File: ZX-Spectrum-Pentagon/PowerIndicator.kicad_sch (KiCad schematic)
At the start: 6 parts

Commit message: prepare for pcb
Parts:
- DPI1: value (none) -> RED; footprint (none) -> LED_SMD:LED_0805_2012Metric_Pad1.15x1.40mm_HandSolder
- DPI2: value (none) -> YELLO; footprint (none) -> LED_SMD:LED_0805_2012Metric_Pad1.15x1.40mm_HandSolder
- DPI3: value (none) -> GREEN; footprint (none) -> LED_SMD:LED_0805_2012Metric_Pad1.15x1.40mm_HandSolder
- RPI1, RPI2, RPI3: value (none) -> 330; footprint (none) -> Resistor_SMD:R_0805_2012Metric_Pad1.20x1.40mm_HandSolder
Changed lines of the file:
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@@
       (effects (font (size 1.27 1.27)) (justify left))
     )
-    (property "Value" "" (id 1) (at 39.878 70.993 0)
+    (property "Value" "330" (id 1) (at 39.878 70.993 0)
       (effects (font (size 1.27 1.27)) (justify left))
     )
-    (property "Footprint" "" (id 2) (at 36.322 69.85 90)
+    (property "Footprint" "Resistor_SMD:R_0805_2012Metric_Pad1.20x1.40mm_HandSolder" (id 2) (at 36.322 69.85 90)
       (effects (font (size 1.27 1.27)) hide)
     )
@@
       (effects (font (size 1.27 1.27)) (justify left))
     )
-    (property "Value" "" (id 1) (at 52.578 70.993 0)
+    (property "Value" "330" (id 1) (at 52.578 70.993 0)
       (effects (font (size 1.27 1.27)) (justify left))
     )
-    (property "Footprint" "" (id 2) (at 49.022 69.85 90)
+    (property "Footprint" "Resistor_SMD:R_0805_2012Metric_Pad1.20x1.40mm_HandSolder" (id 2) (at 49.022 69.85 90)
       (effects (font (size 1.27 1.27)) hide)
     )
@@
       (effects (font (size 1.27 1.27)) (justify left))
     )
-    (property "Value" "" (id 1) (at 65.278 70.993 0)
+    (property "Value" "330" (id 1) (at 65.278 70.993 0)
       (effects (font (size 1.27 1.27)) (justify left))
     )
-    (property "Footprint" "" (id 2) (at 61.722 69.85 90)
+    (property "Footprint" "Resistor_SMD:R_0805_2012Metric_Pad1.20x1.40mm_HandSolder" (id 2) (at 61.722 69.85 90)
       (effects (font (size 1.27 1.27)) hide)
     )
@@
       (effects (font (size 1.27 1.27)) (justify right))
     )
-    (property "Value" "" (id 1) (at 41.0972 58.4708 90)
+    (property "Value" "RED" (id 1) (at 41.0972 58.4708 90)
       (effects (font (size 1.27 1.27)) (justify right))
     )
-    (property "Footprint" "" (id 2) (at 38.1 57.15 0)
+    (property "Footprint" "LED_SMD:LED_0805_2012Metric_Pad1.15x1.40mm_HandSolder" (id 2) (at 38.1 57.15 0)
       (effects (font (size 1.27 1.27)) hide)
     )
@@
       (effects (font (size 1.27 1.27)) (justify right))
     )
-    (property "Value" "" (id 1) (at 53.7972 58.4708 90)
+    (property "Value" "YELLO" (id 1) (at 53.7972 58.4708 90)
       (effects (font (size 1.27 1.27)) (justify right))
     )
-    (property "Footprint" "" (id 2) (at 50.8 57.15 0)
+    (property "Footprint" "LED_SMD:LED_0805_2012Metric_Pad1.15x1.40mm_HandSolder" (id 2) (at 50.8 57.15 0)
       (effects (font (size 1.27 1.27)) hide)
     )
@@
       (effects (font (size 1.27 1.27)) (justify right))
     )
-    (property "Value" "" (id 1) (at 66.4972 58.4708 90)
+    (property "Value" "GREEN" (id 1) (at 66.4972 58.4708 90)
       (effects (font (size 1.27 1.27)) (justify right))
     )
-    (property "Footprint" "" (id 2) (at 63.5 57.15 0)
+    (property "Footprint" "LED_SMD:LED_0805_2012Metric_Pad1.15x1.40mm_HandSolder" (id 2) (at 63.5 57.15 0)
       (effects (font (size 1.27 1.27)) hide)
     )

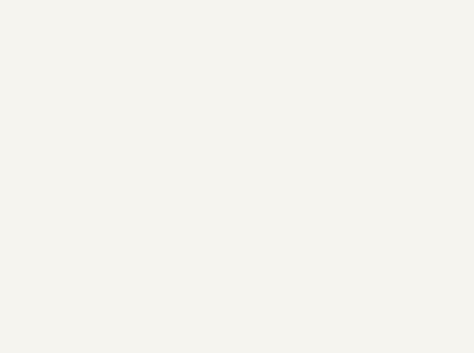
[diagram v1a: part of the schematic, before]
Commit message: tracing VideoEnconer module reconnect PLD tracing VideoFormating module
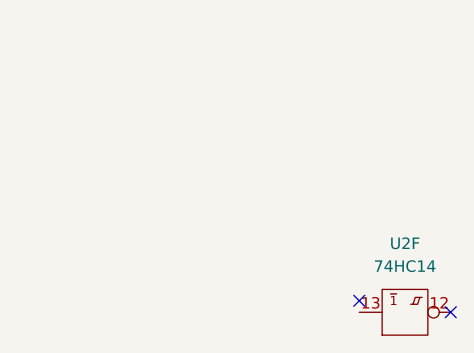
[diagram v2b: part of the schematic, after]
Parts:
- added U2: 74HC14, Package_DIP:DIP-14_W7.62mm, symbol 74IEC:74HC14
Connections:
- net GND: now also U2.7 (GND)
- net VCC: now also U2.14 (VCC)
- no-connect marks 0 -> 2
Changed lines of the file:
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@@
   (junction (at 50.8 76.2) (diameter 0) (color 0 0 0 0)
   )
+  (no_connect (at 77.47 125.73))
+  (no_connect (at 67.31 124.46))
   (wire (pts (xy 50.8 38.1) (xy 50.8 53.34))
     (stroke (width 0) (type default) (color 0 0 0 0))
@@
     (pin "2")
   )
+  (symbol (lib_id "74IEC:74HC14") (at 72.39 125.73 0) (unit 6)
+    (in_bom yes) (on_board yes) (fields_autoplaced)
+    (property "Reference" "U2" (id 0) (at 72.39 118.11 0))
+    (property "Value" "74HC14" (id 1) (at 72.39 120.65 0))
+    (property "Footprint" "Package_DIP:DIP-14_W7.62mm" (id 2) (at 72.39 120.396 0)
+      (effects (font (size 1.27 1.27)) hide)
+    )
+    (property "Datasheet" "https://www.ti.com/lit/ug/scyd013b/scyd013b.pdf" (id 3) (at 72.39 120.396 0)
+      (effects (font (size 1.27 1.27)) hide)
+    )
+    (pin "14")
+    (pin "7")
+    (pin "1")
+    (pin "2")
+    (pin "3")
+    (pin "4")
+    (pin "5")
+    (pin "6")
+    (pin "8")
+    (pin "9")
+    (pin "10")
+    (pin "11")
+    (pin "12")
+    (pin "13")
+  )
 )

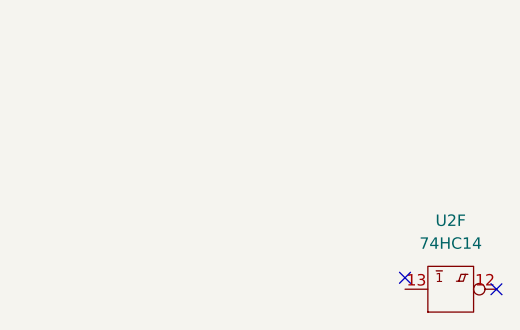
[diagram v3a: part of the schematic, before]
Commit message: fix unused element sepatate network video encoder
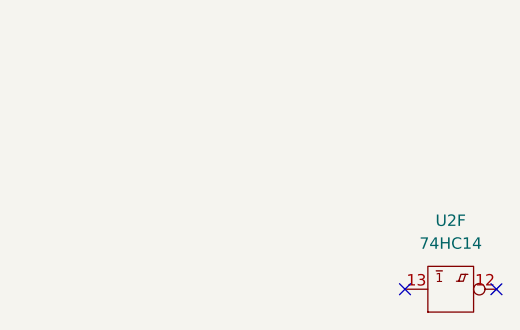
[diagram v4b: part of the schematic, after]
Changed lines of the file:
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@@
   )
   (no_connect (at 77.47 125.73))
-  (no_connect (at 67.31 124.46))
+  (no_connect (at 67.31 125.73))
   (wire (pts (xy 50.8 38.1) (xy 50.8 53.34))
     (stroke (width 0) (type default) (color 0 0 0 0))

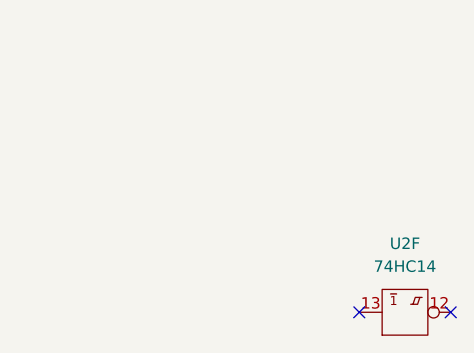
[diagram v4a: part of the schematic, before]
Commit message: FIX rgb add selector 4FSC/FSC
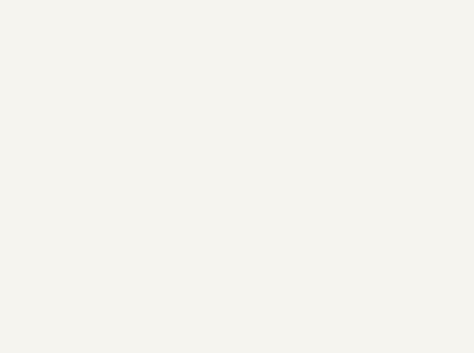
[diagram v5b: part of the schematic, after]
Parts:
- removed U2: 74HC14, Package_DIP:DIP-14_W7.62mm, symbol 74IEC:74HC14
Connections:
- no-connect marks 2 -> 0
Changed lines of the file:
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@@
   (junction (at 50.8 76.2) (diameter 0) (color 0 0 0 0)
   )
-  (no_connect (at 77.47 125.73))
-  (no_connect (at 67.31 125.73))
   (wire (pts (xy 50.8 38.1) (xy 50.8 53.34))
     (stroke (width 0) (type default) (color 0 0 0 0))
@@
     (pin "2")
   )
-  (symbol (lib_id "74IEC:74HC14") (at 72.39 125.73 0) (unit 6)
-    (in_bom yes) (on_board yes) (fields_autoplaced)
-    (property "Reference" "U2" (id 0) (at 72.39 118.11 0))
-    (property "Value" "74HC14" (id 1) (at 72.39 120.65 0))
-    (property "Footprint" "Package_DIP:DIP-14_W7.62mm" (id 2) (at 72.39 120.396 0)
-      (effects (font (size 1.27 1.27)) hide)
-    )
-    (property "Datasheet" "https://www.ti.com/lit/ug/scyd013b/scyd013b.pdf" (id 3) (at 72.39 120.396 0)
-      (effects (font (size 1.27 1.27)) hide)
-    )
-    (pin "14")
-    (pin "7")
-    (pin "1")
-    (pin "2")
-    (pin "3")
-    (pin "4")
-    (pin "5")
-    (pin "6")
-    (pin "8")
-    (pin "9")
-    (pin "10")
-    (pin "11")
-    (pin "12")
-    (pin "13")
-  )
 )

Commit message: reset annotate
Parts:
- renumbered DPI1 to DPI?, DPI2 to DPI?, DPI3 to DPI?, RPI1 to RPI?, RPI2 to RPI?, RPI3 to RPI?
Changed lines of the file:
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@@
   (symbol (lib_id "Device:R") (at 38.1 69.85 0) (unit 1)
     (in_bom yes) (on_board yes)
-    (property "Reference" "RPI1" (id 0) (at 39.878 68.6816 0)
+    (property "Reference" "RPI?" (id 0) (at 39.878 68.6816 0)
       (effects (font (size 1.27 1.27)) (justify left))
     )
@@
   (symbol (lib_id "Device:R") (at 50.8 69.85 0) (unit 1)
     (in_bom yes) (on_board yes)
-    (property "Reference" "RPI2" (id 0) (at 52.578 68.6816 0)
+    (property "Reference" "RPI?" (id 0) (at 52.578 68.6816 0)
       (effects (font (size 1.27 1.27)) (justify left))
     )
@@
   (symbol (lib_id "Device:R") (at 63.5 69.85 0) (unit 1)
     (in_bom yes) (on_board yes)
-    (property "Reference" "RPI3" (id 0) (at 65.278 68.6816 0)
+    (property "Reference" "RPI?" (id 0) (at 65.278 68.6816 0)
       (effects (font (size 1.27 1.27)) (justify left))
     )
@@
   (symbol (lib_id "Device:LED") (at 38.1 57.15 90) (unit 1)
     (in_bom yes) (on_board yes)
-    (property "Reference" "DPI1" (id 0) (at 41.0972 56.1594 90)
+    (property "Reference" "DPI?" (id 0) (at 41.0972 56.1594 90)
       (effects (font (size 1.27 1.27)) (justify right))
     )
@@
   (symbol (lib_id "Device:LED") (at 50.8 57.15 90) (unit 1)
     (in_bom yes) (on_board yes)
-    (property "Reference" "DPI2" (id 0) (at 53.7972 56.1594 90)
+    (property "Reference" "DPI?" (id 0) (at 53.7972 56.1594 90)
       (effects (font (size 1.27 1.27)) (justify right))
     )
@@
   (symbol (lib_id "Device:LED") (at 63.5 57.15 90) (unit 1)
     (in_bom yes) (on_board yes)
-    (property "Reference" "DPI3" (id 0) (at 66.4972 56.1594 90)
+    (property "Reference" "DPI?" (id 0) (at 66.4972 56.1594 90)
       (effects (font (size 1.27 1.27)) (justify right))
     )

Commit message: annotate
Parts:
- gave numbers to parts that had none: 6
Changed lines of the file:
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@@
   (symbol (lib_id "Device:R") (at 38.1 69.85 0) (unit 1)
     (in_bom yes) (on_board yes)
-    (property "Reference" "RPI?" (id 0) (at 39.878 68.6816 0)
+    (property "Reference" "RPI1" (id 0) (at 39.878 68.6816 0)
       (effects (font (size 1.27 1.27)) (justify left))
     )
@@
   (symbol (lib_id "Device:R") (at 50.8 69.85 0) (unit 1)
     (in_bom yes) (on_board yes)
-    (property "Reference" "RPI?" (id 0) (at 52.578 68.6816 0)
+    (property "Reference" "RPI2" (id 0) (at 52.578 68.6816 0)
       (effects (font (size 1.27 1.27)) (justify left))
     )
@@
   (symbol (lib_id "Device:R") (at 63.5 69.85 0) (unit 1)
     (in_bom yes) (on_board yes)
-    (property "Reference" "RPI?" (id 0) (at 65.278 68.6816 0)
+    (property "Reference" "RPI3" (id 0) (at 65.278 68.6816 0)
       (effects (font (size 1.27 1.27)) (justify left))
     )
@@
   (symbol (lib_id "Device:LED") (at 38.1 57.15 90) (unit 1)
     (in_bom yes) (on_board yes)
-    (property "Reference" "DPI?" (id 0) (at 41.0972 56.1594 90)
+    (property "Reference" "DPI1" (id 0) (at 41.0972 56.1594 90)
       (effects (font (size 1.27 1.27)) (justify right))
     )
@@
   (symbol (lib_id "Device:LED") (at 50.8 57.15 90) (unit 1)
     (in_bom yes) (on_board yes)
-    (property "Reference" "DPI?" (id 0) (at 53.7972 56.1594 90)
+    (property "Reference" "DPI2" (id 0) (at 53.7972 56.1594 90)
       (effects (font (size 1.27 1.27)) (justify right))
     )
@@
   (symbol (lib_id "Device:LED") (at 63.5 57.15 90) (unit 1)
     (in_bom yes) (on_board yes)
-    (property "Reference" "DPI?" (id 0) (at 66.4972 56.1594 90)
+    (property "Reference" "DPI3" (id 0) (at 66.4972 56.1594 90)
       (effects (font (size 1.27 1.27)) (justify right))
     )

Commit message: merge with master PowerIndicator.kicad_sch ZX-Spectrum-Pentagon.kicad_sch
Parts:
- added H1, H2, H3, H4, H5, H6: MountingHole_Pad, MountingHole:MountingHole_3.2mm_M3_Pad_Via, symbol Mechanical:MountingHole_Pad
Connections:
- net GND: now also H1.1, H2.1, H3.1, H4.1, H5.1, H6.1
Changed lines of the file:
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@@
 (kicad_sch (version 20211123) (generator eeschema)
   (paper "A4")
+  (junction (at 50.8 95.25) (diameter 0) (color 0 0 0 0)
+  )
   (junction (at 38.1 76.2) (diameter 0) (color 0 0 0 0)
   )
+  (junction (at 38.1 95.25) (diameter 0) (color 0 0 0 0)
+  )
   (junction (at 50.8 76.2) (diameter 0) (color 0 0 0 0)
   )
+  (junction (at 44.45 95.25) (diameter 0) (color 0 0 0 0)
+  )
+  (junction (at 25.4 95.25) (diameter 0) (color 0 0 0 0)
+  )
+  (junction (at 31.75 95.25) (diameter 0) (color 0 0 0 0)
+  )
   (wire (pts (xy 50.8 38.1) (xy 50.8 53.34))
     (stroke (width 0) (type default) (color 0 0 0 0))
@@
     (stroke (width 0) (type default) (color 0 0 0 0))
   )
+  (wire (pts (xy 25.4 95.25) (xy 31.75 95.25))
+    (stroke (width 0) (type default) (color 0 0 0 0))
+  )
   (wire (pts (xy 63.5 25.4) (xy 63.5 53.34))
     (stroke (width 0) (type default) (color 0 0 0 0))
@@
     (stroke (width 0) (type default) (color 0 0 0 0))
   )
+  (wire (pts (xy 57.15 95.25) (xy 57.15 92.71))
+    (stroke (width 0) (type default) (color 0 0 0 0))
+  )
   (wire (pts (xy 38.1 76.2) (xy 50.8 76.2))
     (stroke (width 0) (type default) (color 0 0 0 0))
   )
+  (wire (pts (xy 50.8 92.71) (xy 50.8 95.25))
+    (stroke (width 0) (type default) (color 0 0 0 0))
+  )
   (wire (pts (xy 63.5 73.66) (xy 63.5 76.2))
     (stroke (width 0) (type default) (color 0 0 0 0))
   )
+  (wire (pts (xy 31.75 95.25) (xy 38.1 95.25))
+    (stroke (width 0) (type default) (color 0 0 0 0))
+  )
+  (wire (pts (xy 38.1 92.71) (xy 38.1 95.25))
+    (stroke (width 0) (type default) (color 0 0 0 0))
+  )
+  (wire (pts (xy 38.1 95.25) (xy 44.45 95.25))
+    (stroke (width 0) (type default) (color 0 0 0 0))
+  )
   (wire (pts (xy 50.8 60.96) (xy 50.8 66.04))
     (stroke (width 0) (type default) (color 0 0 0 0))
@@
     (stroke (width 0) (type default) (color 0 0 0 0))
   )
+  (wire (pts (xy 44.45 92.71) (xy 44.45 95.25))
+    (stroke (width 0) (type default) (color 0 0 0 0))
+  )
   (wire (pts (xy 50.8 73.66) (xy 50.8 76.2))
     (stroke (width 0) (type default) (color 0 0 0 0))
   )
+  (wire (pts (xy 25.4 92.71) (xy 25.4 95.25))
+    (stroke (width 0) (type default) (color 0 0 0 0))
+  )
   (wire (pts (xy 25.4 76.2) (xy 38.1 76.2))
     (stroke (width 0) (type default) (color 0 0 0 0))
   )
+  (wire (pts (xy 31.75 92.71) (xy 31.75 95.25))
+    (stroke (width 0) (type default) (color 0 0 0 0))
+  )
   (wire (pts (xy 38.1 50.8) (xy 38.1 53.34))
     (stroke (width 0) (type default) (color 0 0 0 0))
   )
   (wire (pts (xy 63.5 60.96) (xy 63.5 66.04))
+    (stroke (width 0) (type default) (color 0 0 0 0))
+  )
+  (wire (pts (xy 25.4 95.25) (xy 25.4 97.79))
+    (stroke (width 0) (type default) (color 0 0 0 0))
+  )
+  (wire (pts (xy 50.8 95.25) (xy 57.15 95.25))
+    (stroke (width 0) (type default) (color 0 0 0 0))
+  )
+  (wire (pts (xy 44.45 95.25) (xy 50.8 95.25))
     (stroke (width 0) (type default) (color 0 0 0 0))
   )
@@
     (pin "2")
   )
+  (symbol (lib_id "power:GND") (at 25.4 97.79 0) (unit 1)
+    (in_bom yes) (on_board yes) (fields_autoplaced)
+    (property "Reference" "#PWR076" (id 0) (at 25.4 104.14 0)
+      (effects (font (size 1.27 1.27)) hide)
+    )
+    (property "Value" "GND" (id 1) (at 25.4 102.87 0))
+    (property "Footprint" "" (id 2) (at 25.4 97.79 0)
+      (effects (font (size 1.27 1.27)) hide)
+    )
+    (property "Datasheet" "" (id 3) (at 25.4 97.79 0)
+      (effects (font (size 1.27 1.27)) hide)
+    )
+    (pin "1")
+  )
+  (symbol (lib_id "Mechanical:MountingHole_Pad") (at 57.15 90.17 0) (unit 1)
+    (in_bom yes) (on_board yes)
+    (property "Reference" "H6" (id 0) (at 55.88 85.09 0)
+      (effects (font (size 1.27 1.27)) (justify left))
+    )
+    (property "Value" "MountingHole_Pad" (id 1) (at 59.69 90.1699 0)
+      (effects (font (size 1.27 1.27)) (justify left) hide)
+    )
+    (property "Footprint" "MountingHole:MountingHole_3.2mm_M3_Pad_Via" (id 2) (at 57.15 90.17 0)
+      (effects (font (size 1.27 1.27)) hide)
+    )
+    (property "Datasheet" "~" (id 3) (at 57.15 90.17 0)
+      (effects (font (size 1.27 1.27)) hide)
+    )
+    (pin "1")
+  )
+  (symbol (lib_id "Mechanical:MountingHole_Pad") (at 31.75 90.17 0) (unit 1)
+    (in_bom yes) (on_board yes)
+    (property "Reference" "H2" (id 0) (at 30.48 85.09 0)
+      (effects (font (size 1.27 1.27)) (justify left))
+    )
+    (property "Value" "MountingHole_Pad" (id 1) (at 34.29 90.1699 0)
+      (effects (font (size 1.27 1.27)) (justify left) hide)
+    )
+    (property "Footprint" "MountingHole:MountingHole_3.2mm_M3_Pad_Via" (id 2) (at 31.75 90.17 0)
+      (effects (font (size 1.27 1.27)) hide)
+    )
+    (property "Datasheet" "~" (id 3) (at 31.75 90.17 0)
+      (effects (font (size 1.27 1.27)) hide)
+    )
+    (pin "1")
+  )
+  (symbol (lib_id "Mechanical:MountingHole_Pad") (at 25.4 90.17 0) (unit 1)
+    (in_bom yes) (on_board yes)
+    (property "Reference" "H1" (id 0) (at 24.13 85.09 0)
+      (effects (font (size 1.27 1.27)) (justify left))
+    )
+    (property "Value" "MountingHole_Pad" (id 1) (at 27.94 90.1699 0)
+      (effects (font (size 1.27 1.27)) (justify left) hide)
+    )
+    (property "Footprint" "MountingHole:MountingHole_3.2mm_M3_Pad_Via" (id 2) (at 25.4 90.17 0)
+      (effects (font (size 1.27 1.27)) hide)
+    )
+    (property "Datasheet" "~" (id 3) (at 25.4 90.17 0)
+      (effects (font (size 1.27 1.27)) hide)
+    )
+    (pin "1")
+  )
+  (symbol (lib_id "Mechanical:MountingHole_Pad") (at 50.8 90.17 0) (unit 1)
+    (in_bom yes) (on_board yes)
+    (property "Reference" "H5" (id 0) (at 49.53 85.09 0)
+      (effects (font (size 1.27 1.27)) (justify left))
+    )
+    (property "Value" "MountingHole_Pad" (id 1) (at 53.34 90.1699 0)
+      (effects (font (size 1.27 1.27)) (justify left) hide)
+    )
+    (property "Footprint" "MountingHole:MountingHole_3.2mm_M3_Pad_Via" (id 2) (at 50.8 90.17 0)
+      (effects (font (size 1.27 1.27)) hide)
+    )
+    (property "Datasheet" "~" (id 3) (at 50.8 90.17 0)
+      (effects (font (size 1.27 1.27)) hide)
+    )
+    (pin "1")
+  )
+  (symbol (lib_id "Mechanical:MountingHole_Pad") (at 38.1 90.17 0) (unit 1)
+    (in_bom yes) (on_board yes)
+    (property "Reference" "H3" (id 0) (at 36.83 85.09 0)
+      (effects (font (size 1.27 1.27)) (justify left))
+    )
+    (property "Value" "MountingHole_Pad" (id 1) (at 40.64 90.1699 0)
+      (effects (font (size 1.27 1.27)) (justify left) hide)
+    )
+    (property "Footprint" "MountingHole:MountingHole_3.2mm_M3_Pad_Via" (id 2) (at 38.1 90.17 0)
+      (effects (font (size 1.27 1.27)) hide)
+    )
+    (property "Datasheet" "~" (id 3) (at 38.1 90.17 0)
+      (effects (font (size 1.27 1.27)) hide)
+    )
+    (pin "1")
+  )
+  (symbol (lib_id "Mechanical:MountingHole_Pad") (at 44.45 90.17 0) (unit 1)
+    (in_bom yes) (on_board yes)
+    (property "Reference" "H4" (id 0) (at 43.18 85.09 0)
+      (effects (font (size 1.27 1.27)) (justify left))
+    )
+    (property "Value" "MountingHole_Pad" (id 1) (at 46.99 90.1699 0)
+      (effects (font (size 1.27 1.27)) (justify left) hide)
+    )
+    (property "Footprint" "MountingHole:MountingHole_3.2mm_M3_Pad_Via" (id 2) (at 44.45 90.17 0)
+      (effects (font (size 1.27 1.27)) hide)
+    )
+    (property "Datasheet" "~" (id 3) (at 44.45 90.17 0)
+      (effects (font (size 1.27 1.27)) hide)
+    )
+    (pin "1")
+  )
 )
